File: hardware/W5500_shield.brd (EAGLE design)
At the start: 160 x 100 mm, 30 parts, among them IC1 WIZ5500, IC2 741G07S0T23-5-HAND, X1 MEGA2560, Y1 25MHz

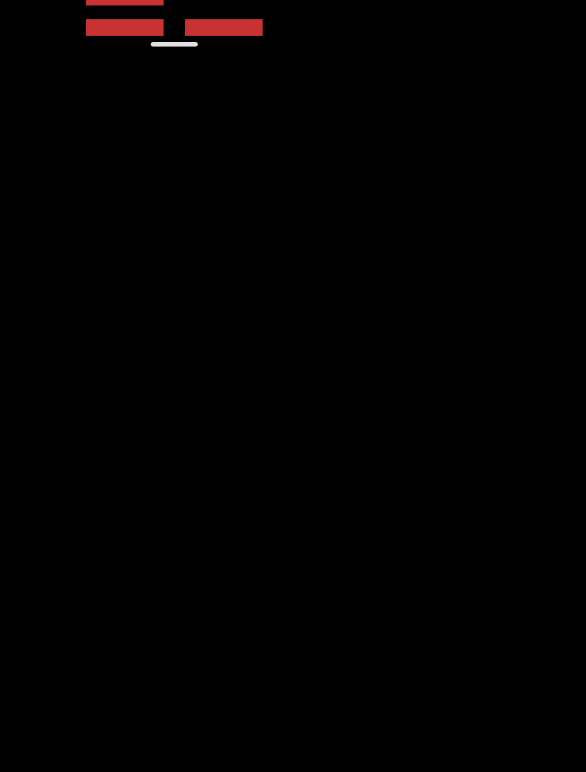
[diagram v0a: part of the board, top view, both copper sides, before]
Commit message: Update W5500 shield
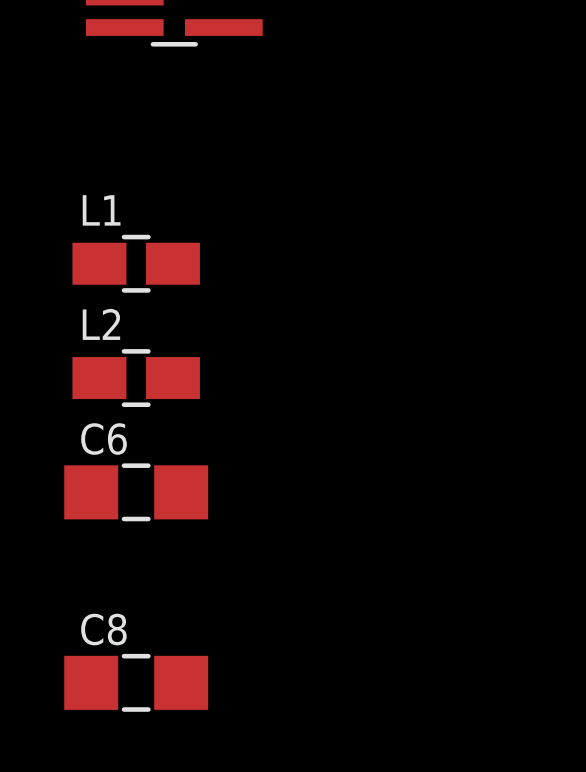
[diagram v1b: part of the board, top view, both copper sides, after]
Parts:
- added C6, C8: 1u, SteveMarple:1206-HAND
- added L1, L2: (no value), SteveMarple:0805-HAND
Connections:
- removed net AGND: IC1.14, IC1.16, IC1.19, IC1.3, IC1.48, IC1.9
- removed net AVDD: IC1.11, IC1.15, IC1.17, IC1.21, IC1.4, IC1.8
- new net +3V3A: C6.1, IC1.11, IC1.15, IC1.17, IC1.21, IC1.4, IC1.8, L1.2
- new net +3V3D: C8.1, IC1.28, L2.2, R10.2, R11.2, R12.2, R2.2, R3.2, R4.2
- net +3V3: now also L1.1, L2.1; no longer IC1.28, R10.2, R11.2, R12.2, R2.2, R3.2, R4.2
- net GND: now also C6.2, C8.2, IC1.14, IC1.16, IC1.19, IC1.3, IC1.48, IC1.9
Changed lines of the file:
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@@
 <element name="U$14" library="SteveMarple" package="PAD" value="PAD" x="91.44" y="43.18" rot="R270"/>
 <element name="U$17" library="SteveMarple" package="PAD" value="PAD" x="91.44" y="7.62"/>
+<element name="L1" library="SteveMarple" package="0805-HAND" value="" x="-88.9" y="-3.81"/>
+<element name="L2" library="SteveMarple" package="0805-HAND" value="" x="-88.9" y="-7.62"/>
+<element name="C6" library="SteveMarple" package="1206-HAND" value="1u" x="-88.9" y="-11.43"/>
+<element name="C8" library="SteveMarple" package="1206-HAND" value="1u" x="-88.9" y="-17.78"/>
 </elements>
 <signals>
-<signal name="AVDD">
-<contactref element="IC1" pad="4"/>
-<contactref element="IC1" pad="8"/>
-<contactref element="IC1" pad="11"/>
-<contactref element="IC1" pad="15"/>
-<contactref element="IC1" pad="17"/>
-<contactref element="IC1" pad="21"/>
-<wire x1="-15.345" y1="57.94" x2="-15.345" y2="58.94" width="0" layer="19" extent="1-1"/>
-<wire x1="-15.345" y1="60.94" x2="-15.345" y2="58.94" width="0" layer="19" extent="1-1"/>
-<wire x1="-18.07" y1="54.715" x2="-15.345" y2="57.94" width="0" layer="19" extent="1-1"/>
-<wire x1="-19.57" y1="54.715" x2="-18.07" y2="54.715" width="0" layer="19" extent="1-1"/>
-<wire x1="-21.57" y1="54.715" x2="-19.57" y2="54.715" width="0" layer="19" extent="1-1"/>
-</signal>
-<signal name="AGND">
-<contactref element="IC1" pad="3"/>
-<contactref element="IC1" pad="9"/>
-<contactref element="IC1" pad="14"/>
-<contactref element="IC1" pad="16"/>
-<contactref element="IC1" pad="19"/>
-<contactref element="IC1" pad="48"/>
-<wire x1="-15.345" y1="57.44" x2="-15.345" y2="58.44" width="0" layer="19" extent="1-1"/>
-<wire x1="-15.345" y1="59.94" x2="-15.345" y2="58.44" width="0" layer="19" extent="1-1"/>
-<wire x1="-19.07" y1="54.715" x2="-15.345" y2="57.44" width="0" layer="19" extent="1-1"/>
-<wire x1="-22.07" y1="54.715" x2="-19.07" y2="54.715" width="0" layer="19" extent="1-1"/>
-<wire x1="-25.295" y1="56.94" x2="-22.07" y2="54.715" width="0" layer="19" extent="1-1"/>
-</signal>
 <signal name="GND">
 <contactref element="IC1" pad="29"/>
@@
 <contactref element="X1" pad="35"/>
 <contactref element="C7" pad="2"/>
-<wire x1="91.44" y1="7.62" x2="90.17" y2="48.031" width="0" layer="19" extent="1-1"/>
-<wire x1="-89.281" y1="4.064" x2="90.17" y2="48.031" width="0" layer="19" extent="1-1"/>
+<contactref element="C8" pad="2"/>
+<contactref element="C6" pad="2"/>
+<contactref element="IC1" pad="3"/>
+<contactref element="IC1" pad="9"/>
+<contactref element="IC1" pad="14"/>
+<contactref element="IC1" pad="16"/>
+<contactref element="IC1" pad="19"/>
+<contactref element="IC1" pad="48"/>
+<wire x1="66.04" y1="25.4" x2="90.17" y2="48.031" width="0" layer="19" extent="1-1"/>
+<wire x1="91.44" y1="7.62" x2="66.04" y2="25.4" width="0" layer="19" extent="1-1"/>
 <wire x1="93.98" y1="7.62" x2="91.44" y2="7.62" width="0" layer="19" extent="1-1"/>
 <wire x1="96.52" y1="7.62" x2="93.98" y2="7.62" width="0" layer="19" extent="1-1"/>
-<wire x1="-80.239" y1="55.88" x2="-89.281" y2="4.064" width="0" layer="19" extent="1-1"/>
-<wire x1="-64.541" y1="69.85" x2="-80.239" y2="55.88" width="0" layer="19" extent="1-1"/>
-<wire x1="-59.461" y1="69.85" x2="-64.541" y2="69.85" width="0" layer="19" extent="1-1"/>
-<wire x1="-54.381" y1="69.85" x2="-59.461" y2="69.85" width="0" layer="19" extent="1-1"/>
-<wire x1="-49.301" y1="69.85" x2="-54.381" y2="69.85" width="0" layer="19" extent="1-1"/>
-<wire x1="-44.221" y1="69.85" x2="-49.301" y2="69.85" width="0" layer="19" extent="1-1"/>
-<wire x1="-29.845" y1="57.15" x2="-44.221" y2="69.85" width="0" layer="19" extent="1-1"/>
-<wire x1="-19.57" y1="64.665" x2="-29.845" y2="57.15" width="0" layer="19" extent="1-1"/>
-<wire x1="-15.345" y1="61.94" x2="-19.57" y2="64.665" width="0" layer="19" extent="1-1"/>
+<wire x1="43.18" y1="2.54" x2="66.04" y2="25.4" width="0" layer="19" extent="1-1"/>
+<wire x1="40.64" y1="2.54" x2="43.18" y2="2.54" width="0" layer="19" extent="1-1"/>
+<wire x1="26.416" y1="50.8" x2="66.04" y2="25.4" width="0" layer="19" extent="1-1"/>
+<wire x1="-15.345" y1="57.44" x2="26.416" y2="50.8" width="0" layer="19" extent="1-1"/>
+<wire x1="-15.345" y1="58.44" x2="-15.345" y2="57.44" width="0" layer="19" extent="1-1"/>
+<wire x1="-15.345" y1="59.94" x2="-15.345" y2="58.44" width="0" layer="19" extent="1-1"/>
+<wire x1="-15.345" y1="61.94" x2="-15.345" y2="59.94" width="0" layer="19" extent="1-1"/>
+<wire x1="-19.07" y1="54.715" x2="-15.345" y2="57.44" width="0" layer="19" extent="1-1"/>
+<wire x1="-22.07" y1="54.715" x2="-19.07" y2="54.715" width="0" layer="19" extent="1-1"/>
+<wire x1="-25.295" y1="56.94" x2="-22.07" y2="54.715" width="0" layer="19" extent="1-1"/>
+<wire x1="-29.845" y1="57.15" x2="-25.295" y2="56.94" width="0" layer="19" extent="1-1"/>
+<wire x1="-19.57" y1="64.665" x2="-15.345" y2="61.94" width="0" layer="19" extent="1-1"/>
 <wire x1="-18.821" y1="69.85" x2="-19.57" y2="64.665" width="0" layer="19" extent="1-1"/>
 <wire x1="-13.741" y1="69.85" x2="-18.821" y2="69.85" width="0" layer="19" extent="1-1"/>
 <wire x1="-23.901" y1="69.85" x2="-18.821" y2="69.85" width="0" layer="19" extent="1-1"/>
 <wire x1="-23.901" y1="73.66" x2="-23.901" y2="69.85" width="0" layer="19" extent="1-1"/>
-<wire x1="26.416" y1="50.8" x2="-13.741" y2="69.85" width="0" layer="19" extent="1-1"/>
-<wire x1="66.04" y1="25.4" x2="26.416" y2="50.8" width="0" layer="19" extent="1-1"/>
-<wire x1="43.18" y1="2.54" x2="66.04" y2="25.4" width="0" layer="19" extent="1-1"/>
-<wire x1="40.64" y1="2.54" x2="43.18" y2="2.54" width="0" layer="19" extent="1-1"/>
+<wire x1="-44.221" y1="69.85" x2="-29.845" y2="57.15" width="0" layer="19" extent="1-1"/>
+<wire x1="-49.301" y1="69.85" x2="-44.221" y2="69.85" width="0" layer="19" extent="1-1"/>
+<wire x1="-54.381" y1="69.85" x2="-49.301" y2="69.85" width="0" layer="19" extent="1-1"/>
+<wire x1="-59.461" y1="69.85" x2="-54.381" y2="69.85" width="0" layer="19" extent="1-1"/>
+<wire x1="-64.541" y1="69.85" x2="-59.461" y2="69.85" width="0" layer="19" extent="1-1"/>
+<wire x1="-80.239" y1="55.88" x2="-64.541" y2="69.85" width="0" layer="19" extent="1-1"/>
+<wire x1="-89.281" y1="4.064" x2="-80.239" y2="55.88" width="0" layer="19" extent="1-1"/>
+<wire x1="-87.401" y1="-11.43" x2="-89.281" y2="4.064" width="0" layer="19" extent="1-1"/>
+<wire x1="-87.401" y1="-17.78" x2="-87.401" y2="-11.43" width="0" layer="19" extent="1-1"/>
 </signal>
 <signal name="PE">
@@
 </signal>
 <signal name="+3V3">
-<contactref element="R2" pad="2"/>
-<contactref element="R4" pad="2"/>
-<contactref element="R3" pad="2"/>
-<contactref element="R10" pad="2"/>
-<contactref element="IC1" pad="28"/>
-<contactref element="R11" pad="2"/>
-<contactref element="R12" pad="2"/>
 <contactref element="U$2" pad="3.3V"/>
-<wire x1="-69.621" y1="69.85" x2="35.56" y2="2.54" width="0" layer="19" extent="1-1"/>
-<wire x1="-74.701" y1="69.85" x2="-69.621" y2="69.85" width="0" layer="19" extent="1-1"/>
-<wire x1="-79.781" y1="69.85" x2="-74.701" y2="69.85" width="0" layer="19" extent="1-1"/>
-<wire x1="-39.141" y1="69.85" x2="-69.621" y2="69.85" width="0" layer="19" extent="1-1"/>
-<wire x1="-34.061" y1="69.85" x2="-39.141" y2="69.85" width="0" layer="19" extent="1-1"/>
-<wire x1="-28.981" y1="69.85" x2="-34.061" y2="69.85" width="0" layer="19" extent="1-1"/>
-<wire x1="-19.07" y1="64.665" x2="-28.981" y2="69.85" width="0" layer="19" extent="1-1"/>
+<contactref element="L1" pad="1"/>
+<contactref element="L2" pad="1"/>
+<wire x1="-90.125" y1="-3.81" x2="-90.125" y2="-7.62" width="0" layer="19" extent="1-1"/>
+<wire x1="35.56" y1="2.54" x2="-90.125" y2="-3.81" width="0" layer="19" extent="1-1"/>
 </signal>
 <signal name="N$14">
@@
 <wire x1="93.98" y1="40.64" x2="91.44" y2="40.64" width="0" layer="19" extent="1-1"/>
 </signal>
+<signal name="+3V3A">
+<contactref element="L1" pad="2"/>
+<contactref element="C6" pad="1"/>
+<contactref element="IC1" pad="15"/>
+<contactref element="IC1" pad="21"/>
+<contactref element="IC1" pad="11"/>
+<contactref element="IC1" pad="17"/>
+<contactref element="IC1" pad="8"/>
+<contactref element="IC1" pad="4"/>
+<wire x1="-87.675" y1="-3.81" x2="-90.399" y2="-11.43" width="0" layer="19" extent="1-1"/>
+<wire x1="-21.57" y1="54.715" x2="-87.675" y2="-3.81" width="0" layer="19" extent="1-1"/>
+<wire x1="-19.57" y1="54.715" x2="-21.57" y2="54.715" width="0" layer="19" extent="1-1"/>
+<wire x1="-18.07" y1="54.715" x2="-19.57" y2="54.715" width="0" layer="19" extent="1-1"/>
+<wire x1="-15.345" y1="57.94" x2="-18.07" y2="54.715" width="0" layer="19" extent="1-1"/>
+<wire x1="-15.345" y1="58.94" x2="-15.345" y2="57.94" width="0" layer="19" extent="1-1"/>
+<wire x1="-15.345" y1="60.94" x2="-15.345" y2="58.94" width="0" layer="19" extent="1-1"/>
+</signal>
+<signal name="+3V3D">
+<contactref element="L2" pad="2"/>
+<contactref element="C8" pad="1"/>
+<contactref element="R2" pad="2"/>
+<contactref element="R4" pad="2"/>
+<contactref element="R3" pad="2"/>
+<contactref element="R10" pad="2"/>
+<contactref element="IC1" pad="28"/>
+<contactref element="R11" pad="2"/>
+<contactref element="R12" pad="2"/>
+<wire x1="-87.675" y1="-7.62" x2="-90.399" y2="-17.78" width="0" layer="19" extent="1-1"/>
+<wire x1="-79.781" y1="69.85" x2="-87.675" y2="-7.62" width="0" layer="19" extent="1-1"/>
+<wire x1="-74.701" y1="69.85" x2="-79.781" y2="69.85" width="0" layer="19" extent="1-1"/>
+<wire x1="-69.621" y1="69.85" x2="-74.701" y2="69.85" width="0" layer="19" extent="1-1"/>
+<wire x1="-39.141" y1="69.85" x2="-69.621" y2="69.85" width="0" layer="19" extent="1-1"/>
+<wire x1="-34.061" y1="69.85" x2="-39.141" y2="69.85" width="0" layer="19" extent="1-1"/>
+<wire x1="-28.981" y1="69.85" x2="-34.061" y2="69.85" width="0" layer="19" extent="1-1"/>
+<wire x1="-19.07" y1="64.665" x2="-28.981" y2="69.85" width="0" layer="19" extent="1-1"/>
+</signal>
 </signals>
